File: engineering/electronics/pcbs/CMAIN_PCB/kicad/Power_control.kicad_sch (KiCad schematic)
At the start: 21 parts, among them K1 CPC1019N, K2 CPC1019N, Q1 SIRA99DP-T1-GE3, Q2 SIRA99DP-T1-GE3

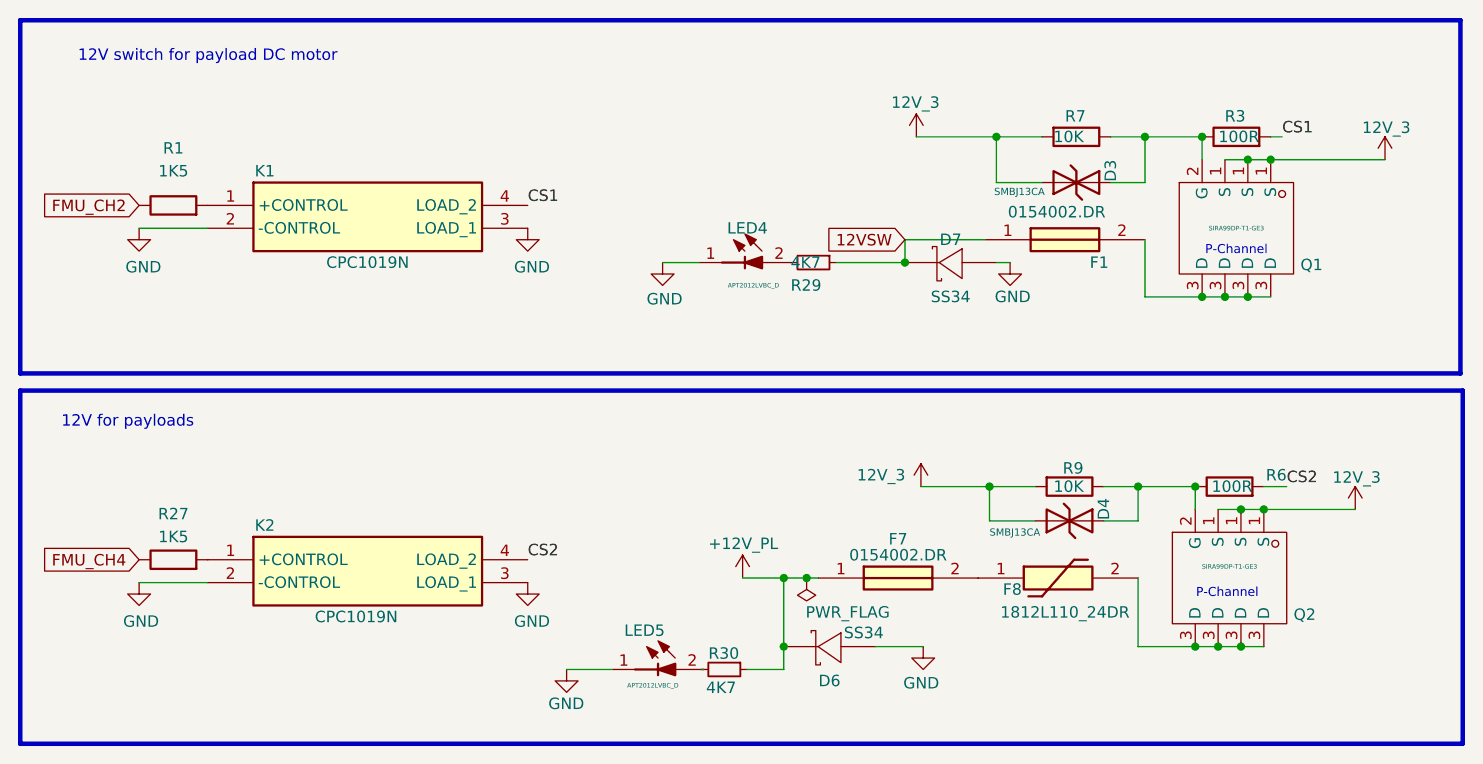
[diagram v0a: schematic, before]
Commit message: Clean up CMAIN part value fields
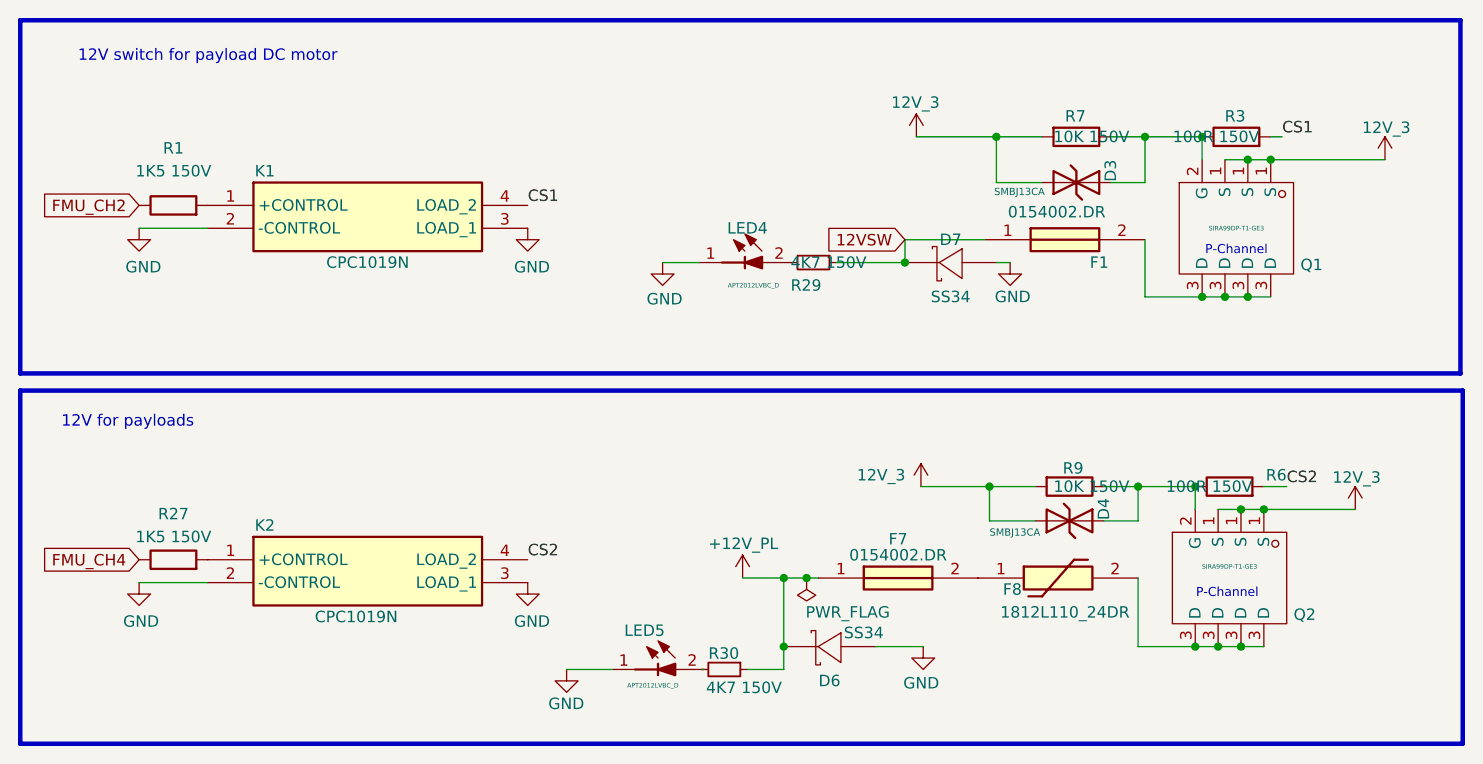
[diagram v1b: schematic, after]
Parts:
- R1, R27: value 1K5 -> 1K5 150V; footprint CMAIN_PCB:fp_9fb50b8536 -> Resistor_SMD:R_0805_2012Metric_Pad1.20x1.40mm_HandSolder
- R29, R30: value 4K7 -> 4K7 150V; footprint CMAIN_PCB:fp_9fb50b8536 -> Resistor_SMD:R_0805_2012Metric_Pad1.20x1.40mm_HandSolder
- R3, R6: value 100R -> 100R 150V; footprint CMAIN_PCB:fp_9fb50b8536 -> Resistor_SMD:R_0805_2012Metric_Pad1.20x1.40mm_HandSolder
- R7, R9: value 10K -> 10K 150V; footprint CMAIN_PCB:fp_9fb50b8536 -> Resistor_SMD:R_0805_2012Metric_Pad1.20x1.40mm_HandSolder

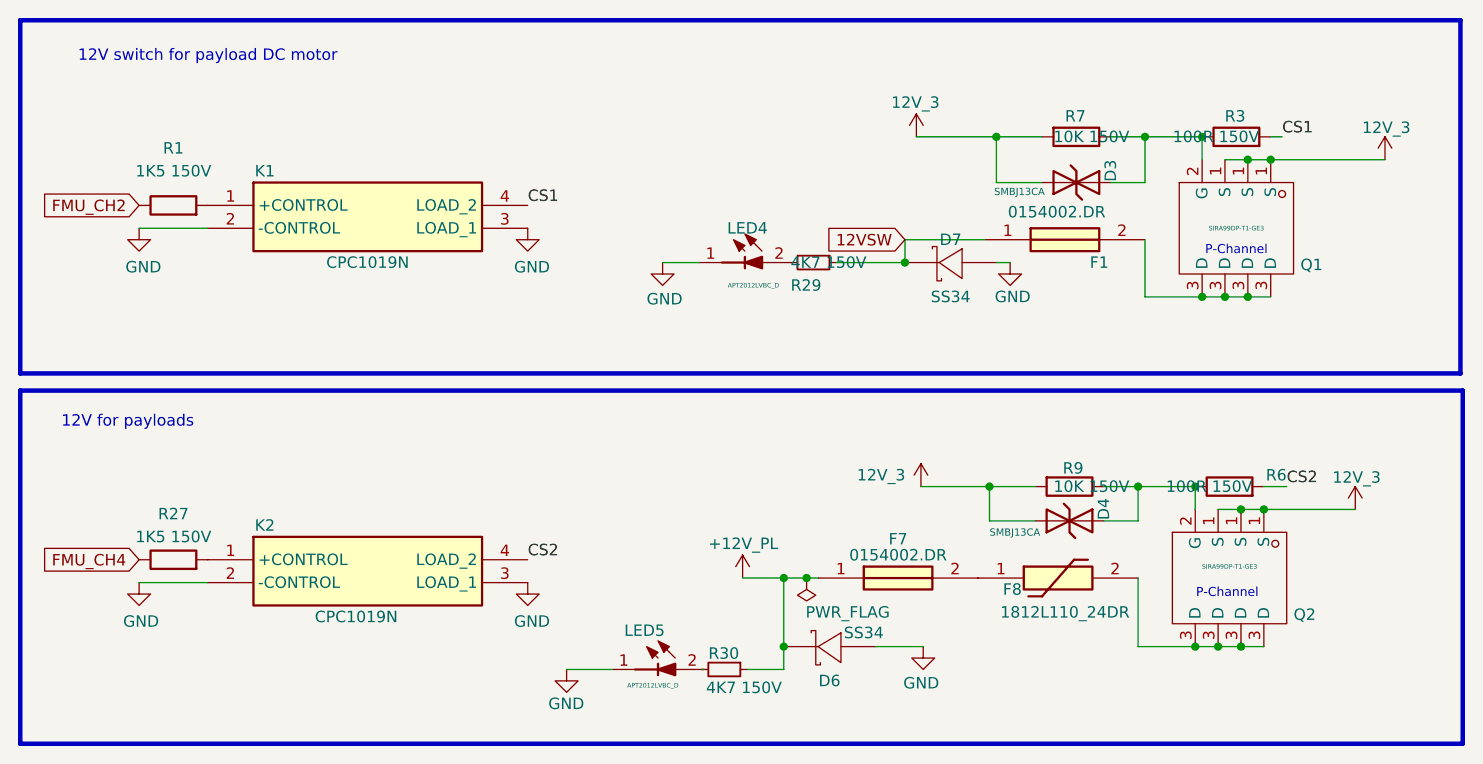
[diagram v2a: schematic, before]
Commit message: fix(cmain): integrate prototype ordering update
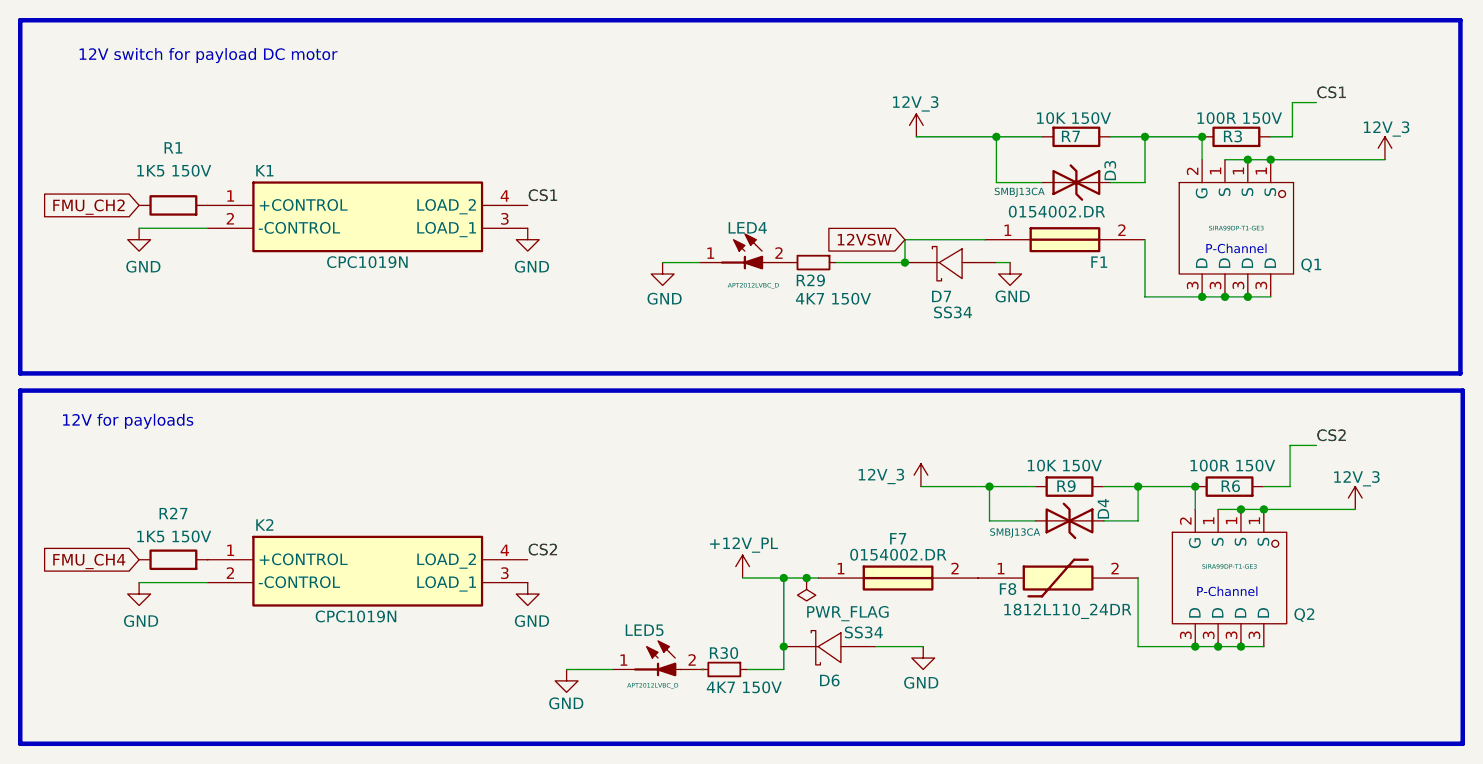
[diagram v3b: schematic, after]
